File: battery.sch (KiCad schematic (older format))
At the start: 14 parts, among them J1 BAT, U1 MCP73831-2-OT, U2 STC3100

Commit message: Add digikey pn's to schematic, update BOM
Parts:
- C1, C2, C33: Digikey (none) -> 311-1439-1-ND
- C3: Digikey (none) -> 311-1035-1-ND
- D1: Digikey (none) -> 160-1448-1-ND
- J1: Digikey (none) -> 455-1749-1-ND
- R1: Digikey (none) -> 311-2KLRCT-ND
- R2: Digikey (none) -> 311-330LRCT-ND
- R3: Digikey (none) -> P124412CT-ND
- R4: Digikey (none) -> 311-1.00KLRCT-ND
- R5: Digikey (none) -> A119933CT-ND
- R6: Digikey (none) -> 311-10.0KLRTR-ND
- U1: Digikey (none) -> MCP73831T-2ATI/OTCT-ND
- U2: Digikey (none) -> 497-10526-1-ND
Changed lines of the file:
@@
 F 3 "~" H 5450 3500 50  0001 C CNN
 F 4 "" V 5450 3500 50  0001 C CNN "LCSC"
+F 5 "455-1749-1-ND" V 5450 3500 50  0001 C CNN "Digikey"
 	1    5450 3500
 	0    -1   -1   0
@@
 F 3 "~" H 1450 3900 50  0001 C CNN
 F 4 "C52923" H 1450 3900 50  0001 C CNN "LCSC"
+F 5 "311-1439-1-ND" H 1450 3900 50  0001 C CNN "Digikey"
 	1    1450 3900
 	1    0    0    -1
@@
 F 3 "~" H 2000 4400 50  0001 C CNN
 F 4 "C4109" H 2000 4400 50  0001 C CNN "LCSC"
+F 5 "311-2KLRCT-ND" H 2000 4400 50  0001 C CNN "Digikey"
 	1    2000 4400
 	1    0    0    -1
@@
 F 3 "~" H 4650 4300 50  0001 C CNN
 F 4 "C52923" H 4650 4300 50  0001 C CNN "LCSC"
+F 5 "311-1439-1-ND" H 4650 4300 50  0001 C CNN "Digikey"
 	1    4650 4300
 	1    0    0    -1
@@
 F 3 "http://ww1.microchip.com/downloads/en/DeviceDoc/20001984g.pdf" H 2800 3950 50  0001 C CNN
 F 4 "C424093" H 2950 4000 50  0001 C CNN "LCSC"
+F 5 "MCP73831T-2ATI/OTCT-ND" H 2950 4000 50  0001 C CNN "Digikey"
 	1    2950 4000
 	1    0    0    -1
@@
 F 3 "~" H 3950 3650 50  0001 C CNN
 F 4 "C72038" V 3950 3650 50  0001 C CNN "LCSC"
+F 5 "160-1448-1-ND" V 3950 3650 50  0001 C CNN "Digikey"
 	1    3950 3650
 	0    -1   -1   0
@@
 F 3 "~" H 3750 4100 50  0001 C CNN
 F 4 "C25104" V 3750 4100 50  0001 C CNN "LCSC"
+F 5 "311-330LRCT-ND" V 3750 4100 50  0001 C CNN "Digikey"
 	1    3750 4100
 	0    1    1    0
@@
 F 2 "jlcpcb_smt:MSOP-8_3x3mm_P0.65mm" H 8050 4350 50  0001 C CNN
 F 3 "" H 8050 4350 50  0001 C CNN
+F 4 "" H 8050 4350 50  0001 C CNN "LCSC"
+F 5 "497-10526-1-ND" H 8050 4350 50  0001 C CNN "Digikey"
 	1    8050 4350
 	-1   0    0    -1
@@
 F 3 "~" H 8950 3900 50  0001 C CNN
 F 4 "C61953" V 8950 3900 50  0001 C CNN "LCSC"
+F 5 "A119933CT-ND" V 8950 3900 50  0001 C CNN "Digikey"
 	1    8950 3900
 	0    -1   1    0
@@
 F 3 "~" H 6850 4100 50  0001 C CNN
 F 4 "C11702" H 6850 4100 50  0001 C CNN "LCSC"
+F 5 "311-1.00KLRCT-ND" H 6850 4100 50  0001 C CNN "Digikey"
 	1    6850 4100
 	1    0    0    -1
@@
 F 3 "~" H 6850 4500 50  0001 C CNN
 F 4 "C16772" H 6850 4500 50  0001 C CNN "LCSC"
+F 5 "311-1035-1-ND" H 6850 4500 50  0001 C CNN "Digikey"
 	1    6850 4500
 	1    0    0    -1
@@
 F 3 "~" H 5550 5000 50  0001 C CNN
 F 4 "C247605" H 5550 5000 50  0001 C CNN "LCSC"
+F 5 "P124412CT-ND" H 5550 5000 50  0001 C CNN "Digikey"
 	1    5550 5000
 	1    0    0    -1
@@
 F 3 "~" H 9800 5100 50  0001 C CNN
 F 4 "C25744" H 9800 5100 50  0001 C CNN "LCSC"
+F 5 "311-10.0KLRTR-ND" H 9800 5100 50  0001 C CNN "Digikey"
 	1    9800 5100
 	1    0    0    -1
@@
 F 3 "~" H 6500 4300 50  0001 C CNN
 F 4 "C52923" H 6500 4300 50  0001 C CNN "LCSC"
+F 5 "311-1439-1-ND" H 6500 4300 50  0001 C CNN "Digikey"
 	1    6500 4300
 	1    0    0    -1
@@
 	6500 4450 6500 4500
 $Comp
-L Graphic:Logo_Open_Hardware_Small #LOGO?
+L Graphic:Logo_Open_Hardware_Small #LOGO8
 U 1 1 5DD41305
 P 10900 6900
-F 0 "#LOGO?" H 10900 7175 50  0001 C CNN
+F 0 "#LOGO8" H 10900 7175 50  0001 C CNN
 F 1 "Logo_Open_Hardware_Small" H 10900 6675 50  0001 C CNN
 F 2 "" H 10900 6900 50  0001 C CNN
@@
 $EndComp
 $Comp
-L Graphic:SYM_Radio_Waves_Large #SYM?
+L Graphic:SYM_Radio_Waves_Large #SYM8
 U 1 1 5DD4130B
 P 10350 6850
-F 0 "#SYM?" H 10350 7050 50  0001 C CNN
+F 0 "#SYM8" H 10350 7050 50  0001 C CNN
 F 1 "SYM_Radio_Waves_Large" H 10350 6600 50  0001 C CNN
 F 2 "" H 10350 6650 50  0001 C CNN

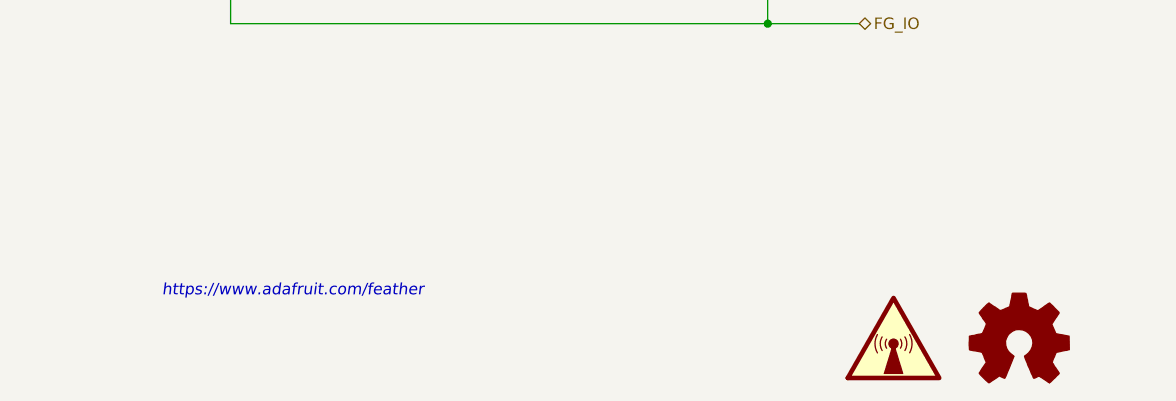
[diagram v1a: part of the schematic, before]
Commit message: PCB REV C0 * Make U8 footprint capable of crypto and fram device * Minor updates to schematic * Minor updates to doc prints * Update bot silk to REV C0
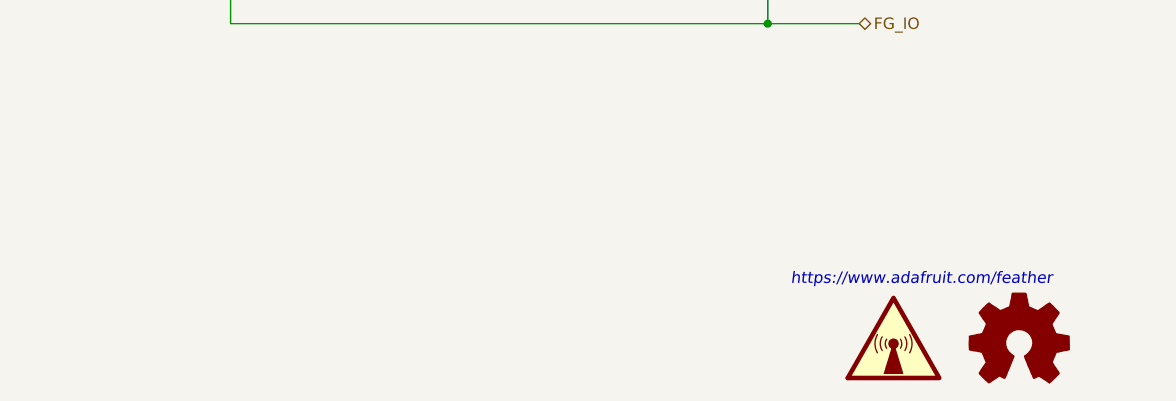
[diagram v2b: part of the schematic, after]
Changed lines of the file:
@@
 EndData
 $EndBitmap
-Text Notes 7150 6700 0    50   Italic 0
+Text Notes 9900 6650 0    50   Italic 0
 https://www.adafruit.com/feather
 $Bitmap
